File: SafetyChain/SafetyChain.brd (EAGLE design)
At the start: 100 x 80 mm, 5 parts, among them T1 BTA26-H

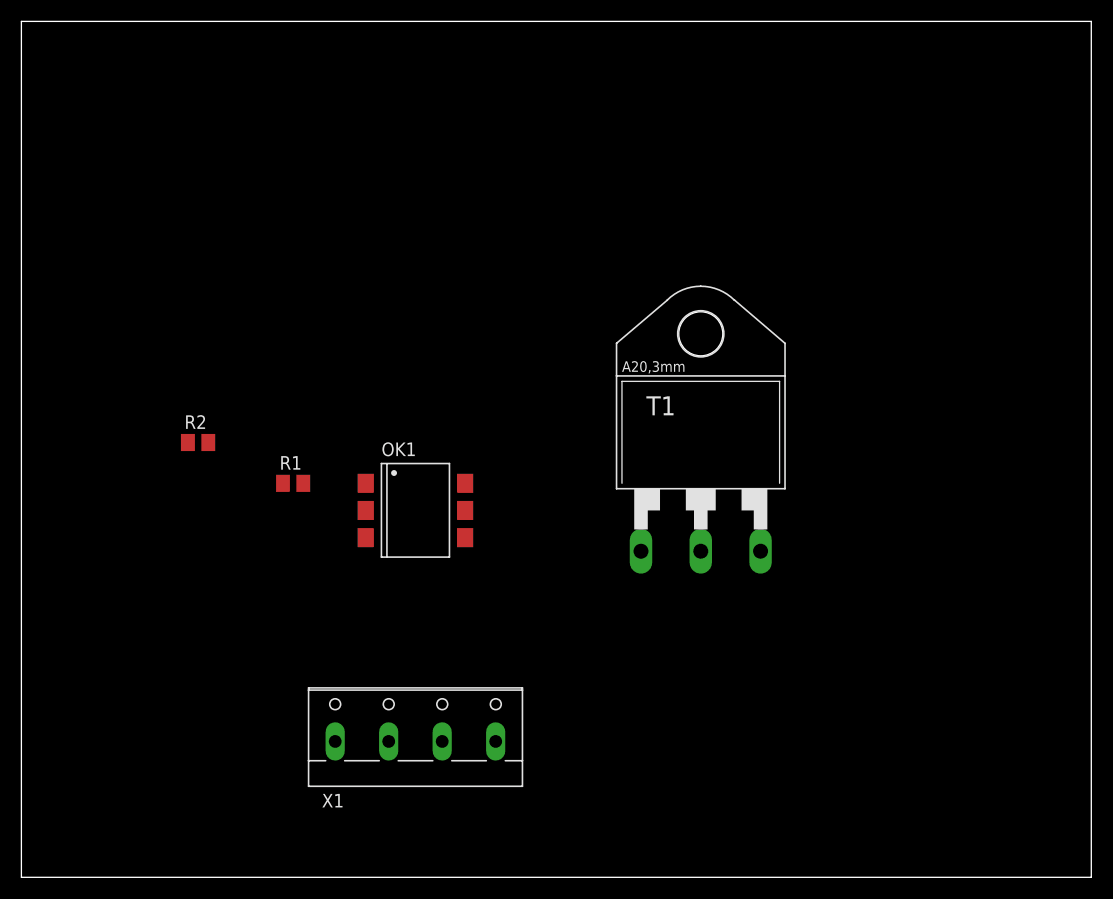
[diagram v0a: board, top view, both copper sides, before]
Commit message: Re-routed a display pin to have the whole display on ports B and C. Safety chain board layouted.
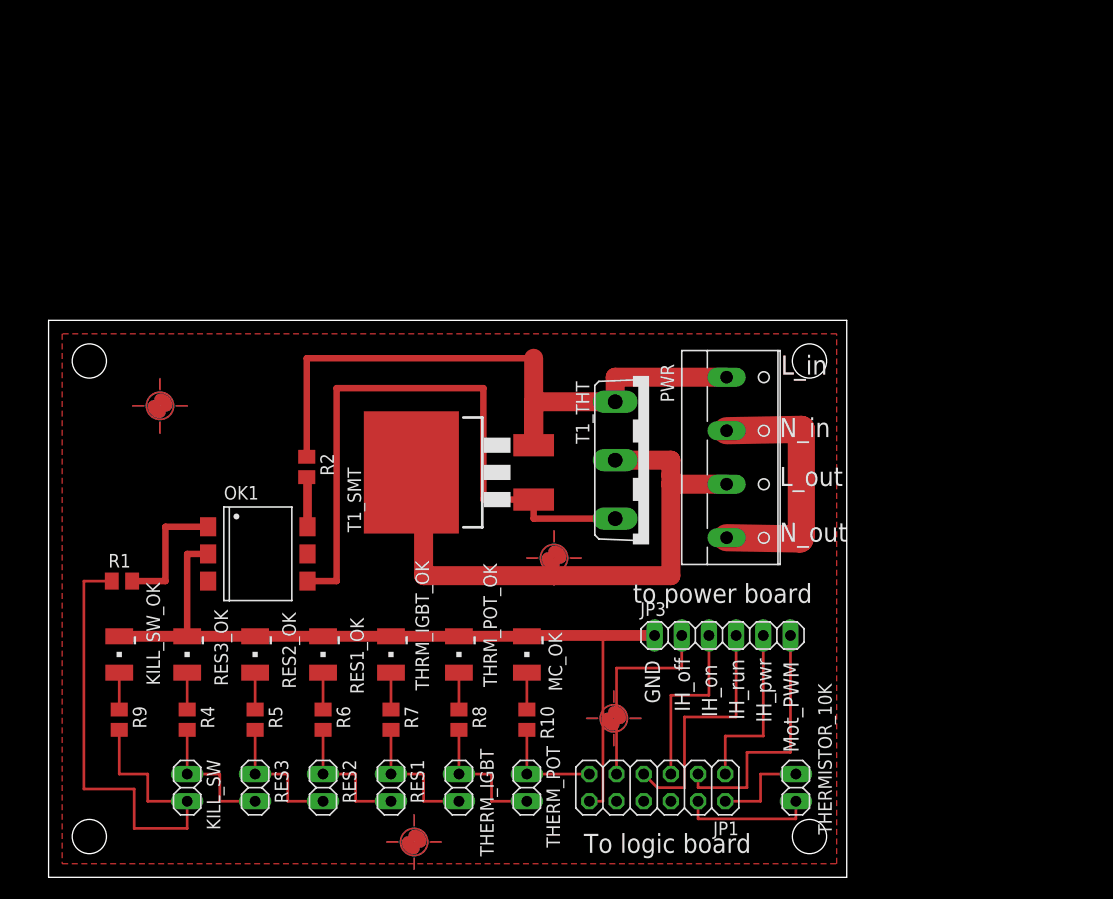
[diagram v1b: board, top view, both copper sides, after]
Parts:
- removed T1: BTA26-H, triac:TOP3L-1
- removed X1: (no value), con-wago-500:W237-4
- added JP1: (no value), pinhead:2X06
- added JP3: (no value), pinhead:1X06
- added KILL_SW, RES1, RES2, RES3, THERMISTOR_10K, THERM_IGBT, THERM_POT: (no value), pinhead:1X02
- added KILL_SW_OK, MC_OK, RES1_OK, RES2_OK, RES3_OK, THRM_IGBT_OK, THRM_POT_OK: LG_T679-E1F1-1, led:PLCC2
- added PWR: (no value), con-wago-500:W237-4
- added R10, R4, R5, R6, R7, R8, R9: 819, rcl:M0805
- added T1_SMT: BTA26-V, transistor-power:D2PACK
- added T1_THT: BTA26-V, triac:TOP3S-1
- added U$1, U$2, U$3, U$4: (no value), marks:PASS-ROUND
- moved R1 18.4 mm to (9.40, 27.7)
- moved OK1 15.3 mm to (22.1, 30.2)
- moved R2 10.4 mm to (26.7, 38.4), turned to 270 degrees
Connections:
- new net 3V3: JP1.4, THERMISTOR_10K.2
- new net GND: JP1.12, JP3.1, KILL_SW_OK.C, MC_OK.C, OK1.2, RES1_OK.C, RES2_OK.C, RES3_OK.C, THRM_IGBT_OK.C, THRM_POT_OK.C
- new net IH_OFF: JP1.9, JP3.2
- new net IH_ON: JP1.5, JP3.3
- new net IH_PWR: JP1.1, JP3.5
- new net IH_RUN: JP1.7, JP3.4
- new net IH_THERMISTOR: JP1.2, THERMISTOR_10K.1
- new net L_IN: PWR.1, R2.1, T1_SMT.3, T1_THT.A1
- new net L_OUT: PWR.3, T1_SMT.2, T1_THT.A2
- new net MOT_PWM: JP1.3, JP3.6
- new net N$10: R5.1, RES2_OK.A
- new net N$11: R6.1, RES1_OK.A
- new net N$12: R7.1, THRM_IGBT_OK.A
- new net N$13: R8.1, THRM_POT_OK.A
- new net N$14: MC_OK.A, R10.1
- new net N$15: KILL_SW_OK.A, R9.1
- new net N$2: OK1.6, R2.2
- new net N$3: R8.2, THERM_IGBT.1, THERM_POT.2
- new net N$4: R7.2, RES1.1, THERM_IGBT.2
- new net N$5: R6.2, RES1.2, RES2.1
- new net N$6: R5.2, RES2.2, RES3.1
- new net N$7: KILL_SW.1, R4.2, RES3.2
- new net N$8: KILL_SW.2, R1.1, R9.2
- new net N$9: R4.1, RES3_OK.A
- new net PWR_N: PWR.2, PWR.4
- new net SAFETY_OK: JP1.11, R10.2, THERM_POT.1
- new net TRIAC_DRV: OK1.4, T1_SMT.1, T1_THT.G
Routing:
- net GND: track 0.00 -> 77.1 mm
- net L_IN: track 0.00 -> 62.9 mm
- net TRIAC_DRV: track 0.00 -> 59.0 mm
- net L_OUT: track 0.00 -> 55.1 mm
- net N$8: track 0.00 -> 50.9 mm
- net MOT_PWM: track 0.00 -> 24.1 mm
- net PWR_N: track 0.00 -> 24.1 mm
- net IH_RUN: track 0.00 -> 23.4 mm
- net IH_OFF: track 0.00 -> 19.1 mm
- net IH_PWR: track 0.00 -> 16.5 mm
- net IH_ON: track 0.00 -> 16.5 mm
- net N$7: track 0.00 -> 13.0 mm
- net N$4: track 0.00 -> 13.0 mm
- net N$3: track 0.00 -> 13.0 mm
- net N$6: track 0.00 -> 13.0 mm
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- added copper zone on layer 1, net N$16
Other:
- board size 100 x 80 mm -> 74.6 x 52.1 mm
- board text added: "GND"
- board text added: "IH_off"
- board text added: "IH_on"
- board text added: "IH_pwr"
- board text added: "IH_run"
- board text added: "L_in"
- board text added: "L_out"
- board text added: "Mot_PWM"
- board text added: "N_in"
- board text added: "N_out"
- board text added: "To logic board"
- board text added: "to power board"

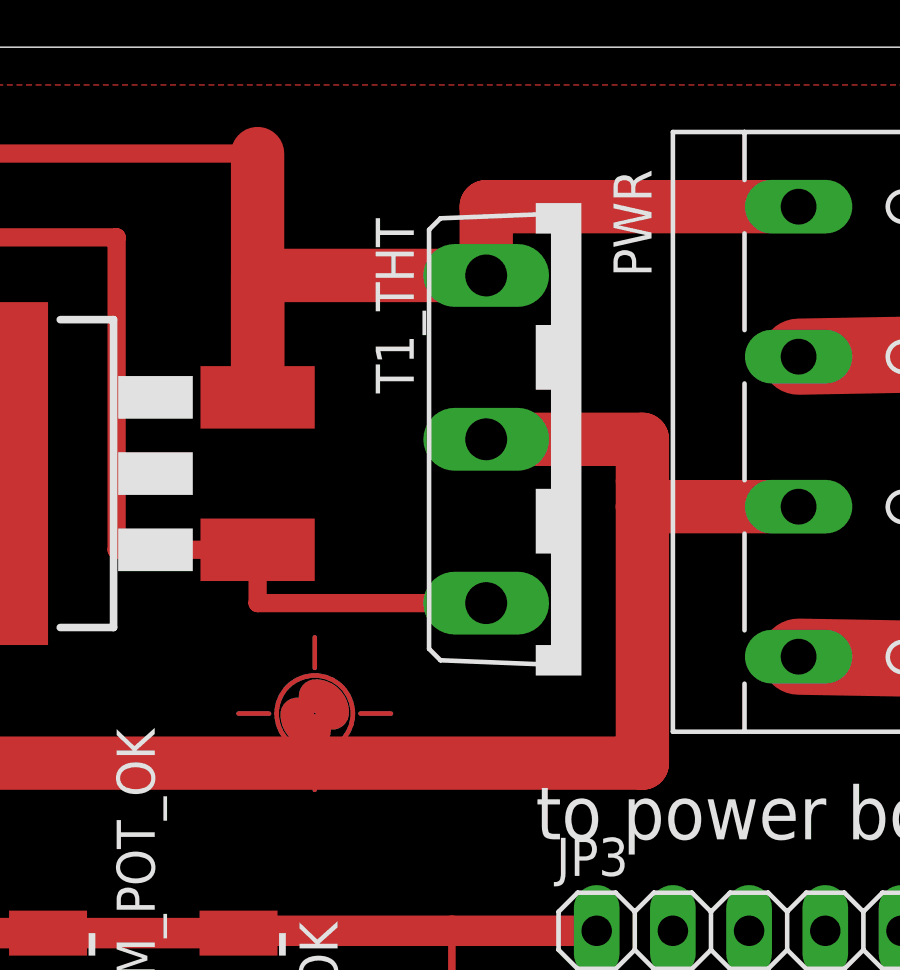
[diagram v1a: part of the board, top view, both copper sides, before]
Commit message: Renamed files.
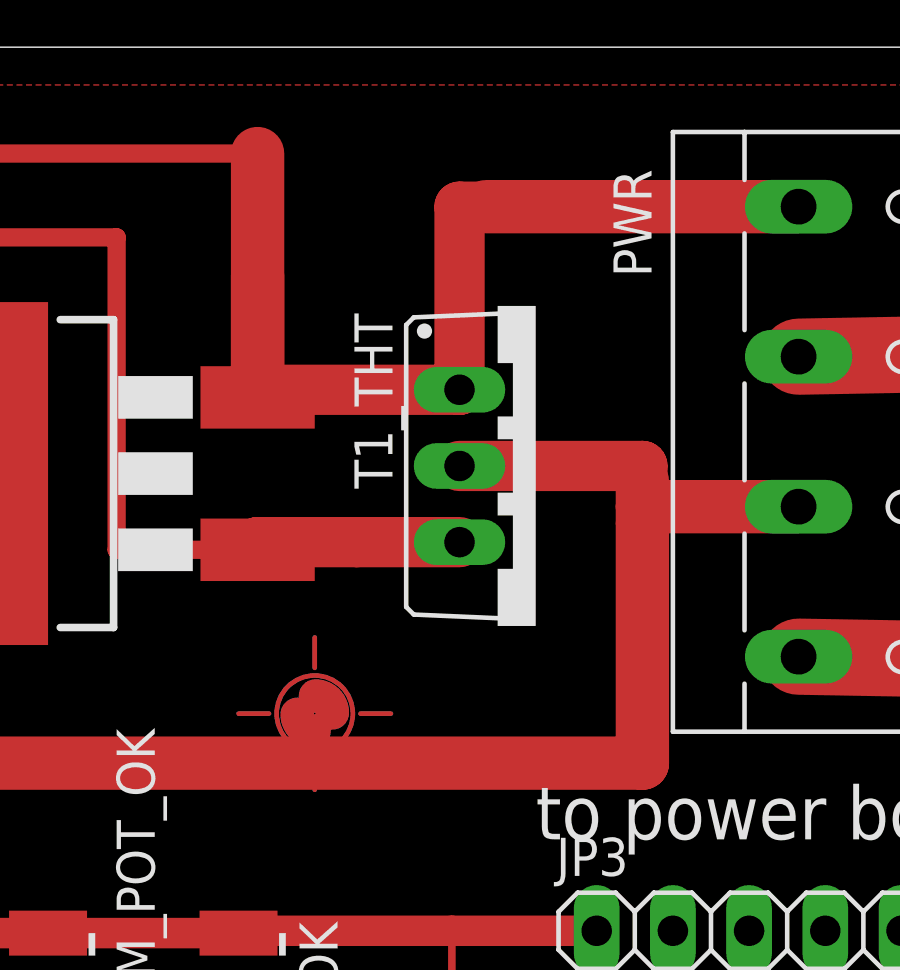
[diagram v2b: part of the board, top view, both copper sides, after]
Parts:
- T1_SMT: value BTA26-V -> BTA16
- T1_THT: value BTA26-V -> BTA16; device triac:TOP3S-1 -> triac:TO220BV
- moved T1_THT 1.76 mm to (57.1, 38.1)
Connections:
- net L_IN: now also T1_THT.T1; no longer T1_THT.A1
- net L_OUT: now also T1_THT.T2; no longer T1_THT.A2
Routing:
- net L_IN: track 62.9 -> 67.0 mm
- net TRIAC_DRV: track 59.0 -> 59.9 mm
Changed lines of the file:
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@@
 </autorouter>
 <elements>
-<element name="T1_THT" library="triac" package="TOP3S-1" value="BTA26-V" x="58.674" y="38.989" rot="R270"/>
 <element name="OK1" library="optocoupler" package="DIL6-SMD" value="MOC3031S" x="22.098" y="30.226" rot="R270">
 <attribute name="OC_NEWARK" value="34C1335" x="-12.192" y="11.176" size="1.778" layer="27" rot="R270" display="off"/>
@@
 <attribute name="VALUE" x="28.321" y="25.4" size="1.27" layer="27"/>
 </element>
-<element name="T1_SMT" library="transistor-power" package="D2PACK" value="BTA26-V" x="38.989" y="37.846" rot="R90"/>
+<element name="T1_SMT" library="transistor-power" package="D2PACK" value="BTA16" x="38.989" y="37.846" rot="R90"/>
 <element name="U$1" library="marks" package="PASS-ROUND" value="" x="12.954" y="44.069"/>
 <element name="U$2" library="marks" package="PASS-ROUND" value="" x="49.784" y="29.845"/>
 <element name="U$3" library="marks" package="PASS-ROUND" value="" x="55.372" y="14.859"/>
 <element name="U$4" library="marks" package="PASS-ROUND" value="" x="36.703" y="3.302"/>
+<element name="T1_THT" library="triac" package="TO220BV" value="BTA16" x="57.15" y="38.1" rot="R270"/>
 </elements>
 <signals>
@@
 <signal name="L_IN">
 <contactref element="PWR" pad="1"/>
-<contactref element="T1_THT" pad="A1"/>
 <contactref element="R2" pad="1"/>
 <contactref element="T1_SMT" pad="3"/>
 <wire x1="65.913" y1="46.743" x2="55.499" y2="46.743" width="1.778" layer="1"/>
-<wire x1="55.499" y1="46.743" x2="55.499" y2="44.45" width="1.778" layer="1"/>
-<wire x1="55.499" y1="44.45" x2="47.879" y2="44.45" width="1.778" layer="1"/>
 <wire x1="47.879" y1="44.45" x2="47.879" y2="40.386" width="1.778" layer="1"/>
 <wire x1="47.879" y1="40.386" x2="47.879" y2="48.514" width="1.778" layer="1"/>
 <wire x1="47.879" y1="48.514" x2="26.67" y2="48.514" width="0.6096" layer="1"/>
 <wire x1="26.67" y1="48.514" x2="26.67" y2="39.304" width="0.6096" layer="1"/>
+<contactref element="T1_THT" pad="T1"/>
+<wire x1="55.499" y1="46.743" x2="54.61" y2="46.743" width="1.6764" layer="1"/>
+<wire x1="54.61" y1="46.743" x2="54.61" y2="40.64" width="1.6764" layer="1"/>
+<wire x1="54.61" y1="40.64" x2="47.879" y2="40.64" width="1.6764" layer="1"/>
+<wire x1="47.879" y1="40.64" x2="47.879" y2="40.386" width="1.6764" layer="1"/>
 </signal>
 <signal name="L_OUT">
-<contactref element="T1_THT" pad="A2"/>
 <contactref element="PWR" pad="3"/>
 <contactref element="T1_SMT" pad="2"/>
 <wire x1="65.913" y1="36.743" x2="60.706" y2="36.743" width="1.778" layer="1"/>
 <wire x1="60.706" y1="36.743" x2="60.706" y2="37.592" width="1.778" layer="1"/>
-<wire x1="60.706" y1="37.592" x2="60.706" y2="38.989" width="1.778" layer="1"/>
-<wire x1="60.706" y1="38.989" x2="55.499" y2="38.989" width="1.778" layer="1"/>
 <wire x1="36.449" y1="37.846" x2="37.592" y2="37.846" width="1.778" layer="1"/>
 <wire x1="37.592" y1="37.846" x2="37.592" y2="28.194" width="1.778" layer="1"/>
 <wire x1="37.592" y1="28.194" x2="60.706" y2="28.194" width="1.778" layer="1"/>
-<wire x1="60.706" y1="28.194" x2="60.706" y2="36.743" width="1.778" layer="1"/>
+<wire x1="60.706" y1="28.194" x2="60.706" y2="36.195" width="1.778" layer="1"/>
+<contactref element="T1_THT" pad="T2"/>
+<wire x1="60.706" y1="36.195" x2="60.706" y2="36.743" width="1.778" layer="1"/>
+<wire x1="54.61" y1="38.1" x2="60.706" y2="38.1" width="1.6764" layer="1"/>
+<wire x1="60.706" y1="38.1" x2="60.706" y2="37.592" width="1.6764" layer="1"/>
 </signal>
 <signal name="TRIAC_DRV">
 <contactref element="OK1" pad="4"/>
-<contactref element="T1_THT" pad="G"/>
 <contactref element="T1_SMT" pad="1"/>
-<wire x1="55.499" y1="33.528" x2="47.879" y2="33.528" width="0.6096" layer="1"/>
-<wire x1="47.879" y1="33.528" x2="47.879" y2="35.306" width="0.6096" layer="1"/>
+<wire x1="51.181" y1="35.56" x2="47.879" y2="35.306" width="0.6096" layer="1"/>
 <wire x1="47.879" y1="35.306" x2="43.18" y2="35.306" width="0.6096" layer="1"/>
 <wire x1="43.18" y1="35.306" x2="43.18" y2="45.72" width="0.6096" layer="1"/>
@@
 <wire x1="29.464" y1="45.72" x2="29.464" y2="27.686" width="0.6096" layer="1"/>
 <wire x1="29.464" y1="27.686" x2="26.743" y2="27.686" width="0.6096" layer="1"/>
+<contactref element="T1_THT" pad="G"/>
+<wire x1="54.61" y1="35.56" x2="51.181" y2="35.56" width="1.6764" layer="1"/>
+<wire x1="51.181" y1="35.56" x2="47.879" y2="35.56" width="1.6764" layer="1"/>
+<wire x1="47.879" y1="35.56" x2="47.879" y2="35.306" width="1.6764" layer="1"/>
 </signal>
 <signal name="N$2">
